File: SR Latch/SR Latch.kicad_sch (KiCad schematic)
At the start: 15 parts, among them J1 Conn_01x02, Q1 BC547, Q2 BC547, Q3 BC547, Q4 BC547, SW1 RESET, SW2 SET

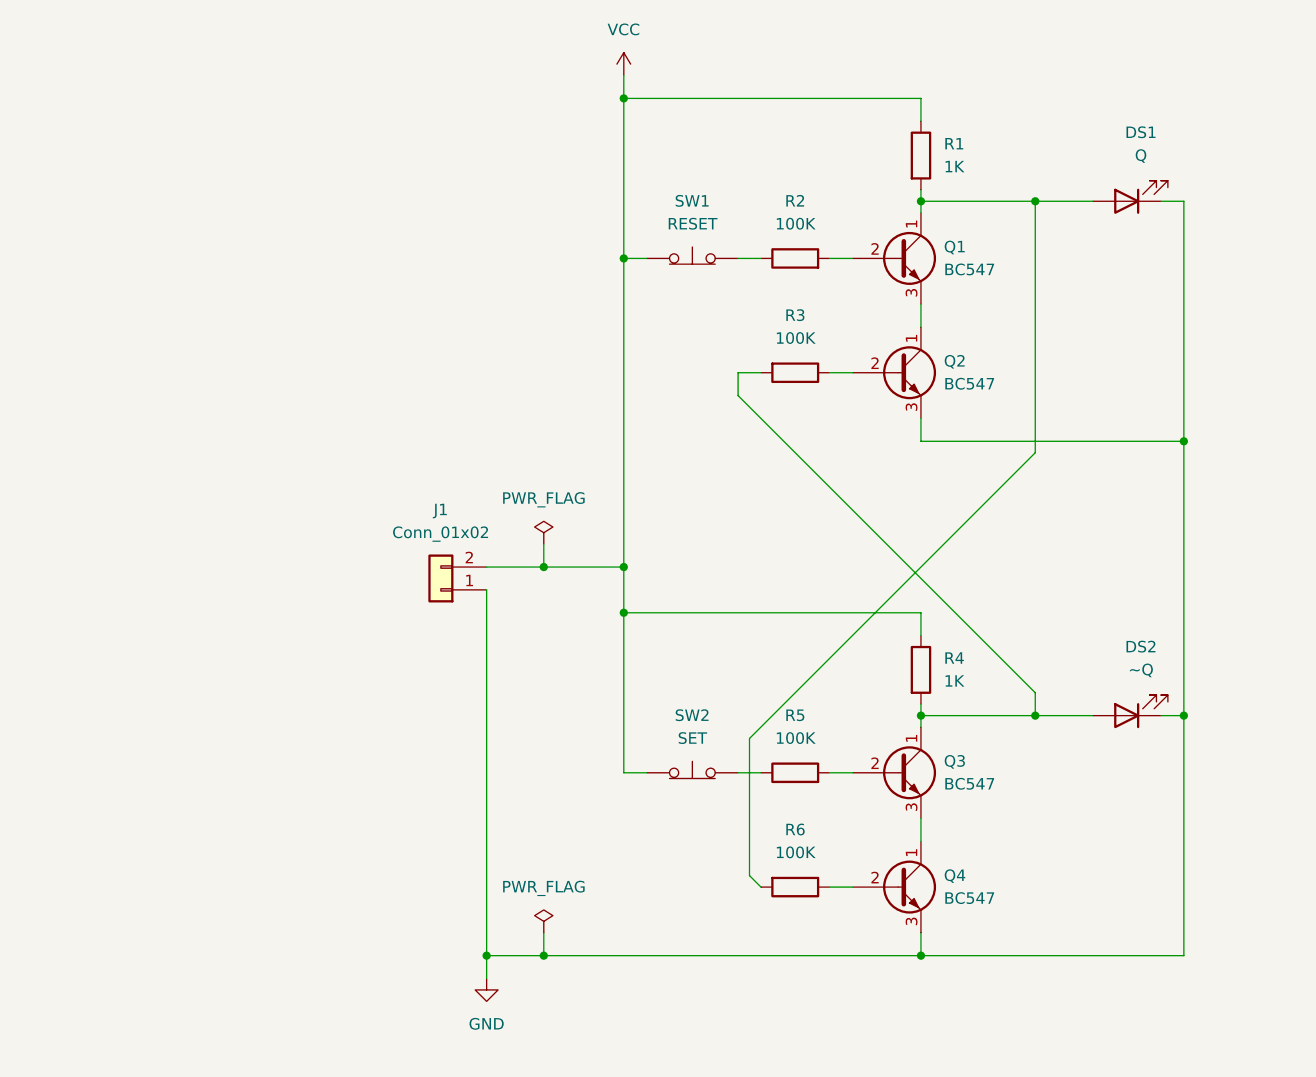
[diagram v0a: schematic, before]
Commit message: fix(SR Latch): Updated resistor values
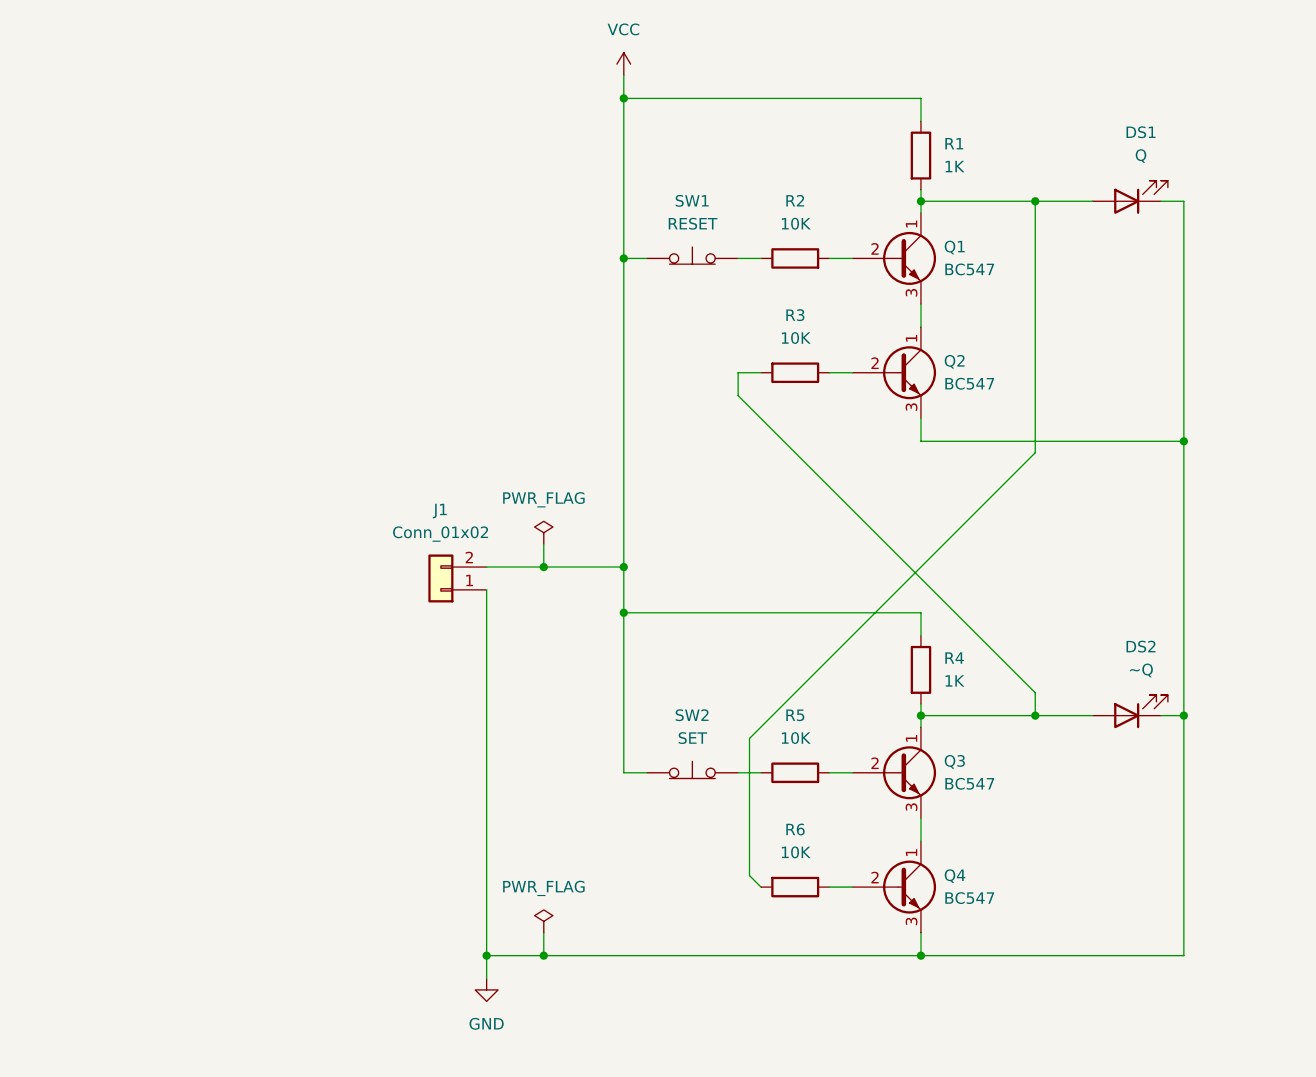
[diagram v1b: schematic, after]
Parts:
- R2, R3, R5, R6: value 100K -> 10K
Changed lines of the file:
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@@
       (effects (font (size 1.27 1.27)))
     )
-    (property "Value" "100K" (at 148.59 127 90)
+    (property "Value" "10K" (at 148.59 127 90)
       (effects (font (size 1.27 1.27)))
     )
@@
       (effects (font (size 1.27 1.27)))
     )
-    (property "Value" "100K" (at 148.59 114.3 90)
+    (property "Value" "10K" (at 148.59 114.3 90)
       (effects (font (size 1.27 1.27)))
     )
@@
       (effects (font (size 1.27 1.27)))
     )
-    (property "Value" "100K" (at 148.59 57.15 90)
+    (property "Value" "10K" (at 148.59 57.15 90)
       (effects (font (size 1.27 1.27)))
     )
@@
       (effects (font (size 1.27 1.27)))
     )
-    (property "Value" "100K" (at 148.59 69.85 90)
-      (effects (font (size 1.27 1.27)))
-    )
+    (property "Value" "10K" (at 148.59 69.85 90)
+      (effects (font (size 1.27 1.27)))
+    )

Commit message: fix: Fixed the SR Latch project (Omron tactile switches)
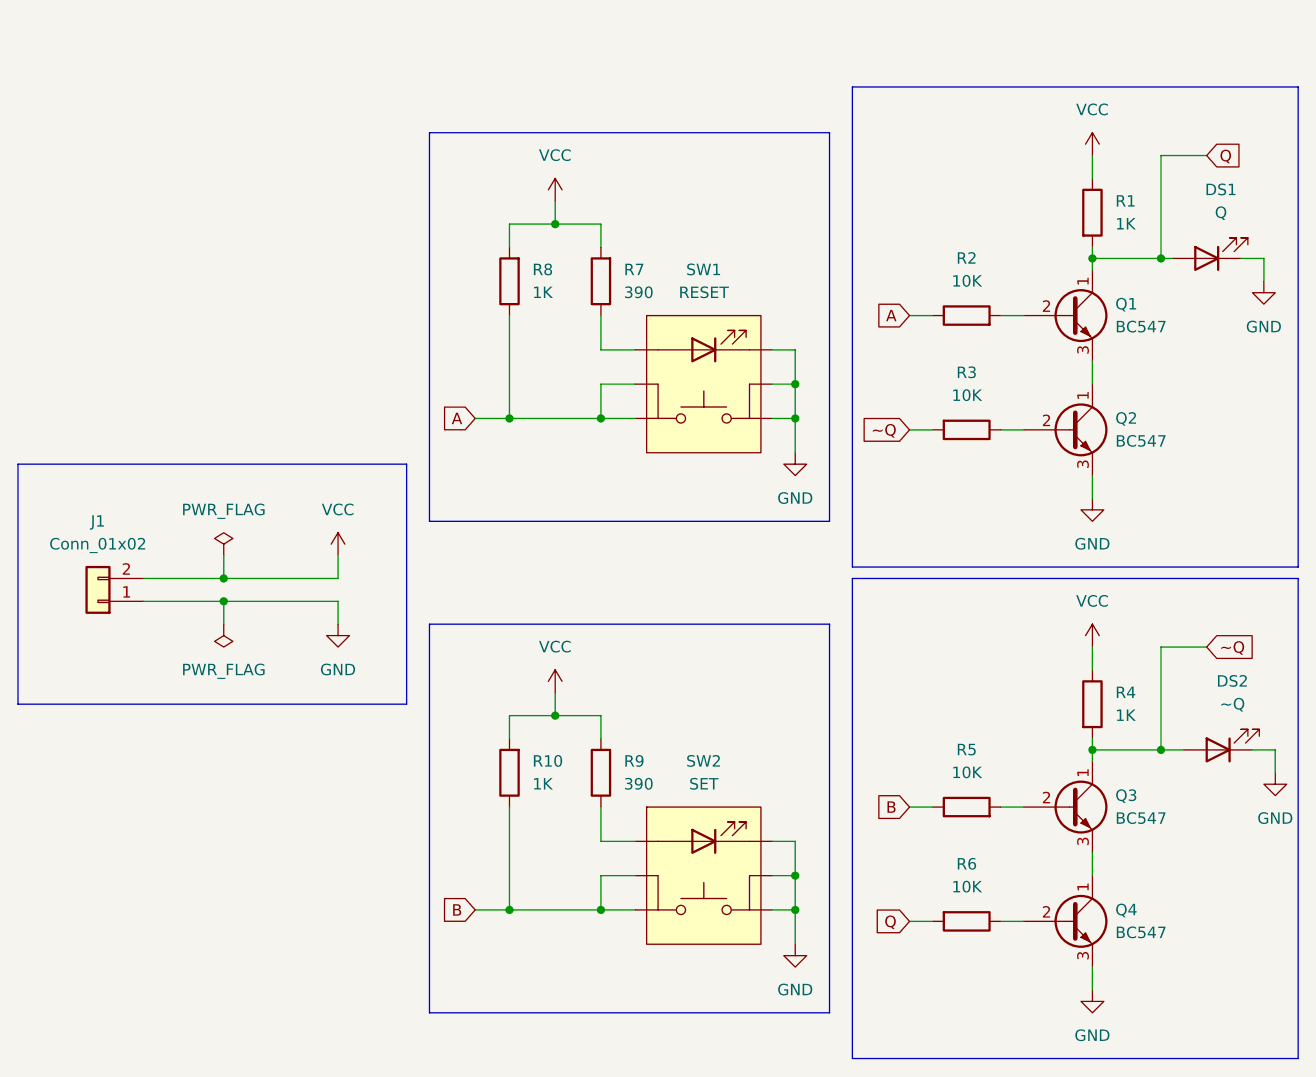
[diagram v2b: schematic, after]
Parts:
- removed SW1: RESET, XS:Tactile-Omrom-B3W-900X-X1X, symbol Switch:SW_Push_Open
- removed SW2: SET, XS:Tactile-Omrom-B3W-900X-X1X, symbol Switch:SW_Push_Open
- added R10, R8: 1K, XS:Resistor-Vishay-CCF07, symbol Device:R
- added R7, R9: 390, XS:Resistor-Vishay-CCF07, symbol Device:R
- added SW1: RESET, XS:Tactile-Omron-B3W-900X-X1X, symbol XS:Tactile-Omron-B3W-900X-X1X
- added SW2: SET, XS:Tactile-Omron-B3W-900X-X1X, symbol XS:Tactile-Omron-B3W-900X-X1X
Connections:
- net GND: now also SW1.1, SW1.2, SW1.5 (K), SW2.1, SW2.2, SW2.5 (K)
- net VCC: now also R10.2, R7.2, R8.2, R9.2
- net Q: now reaches DS1.2 (A), Q1.1 (C), R1.2, R6.2
- net B: now reaches R5.1
- net B: now also R10.1, SW2.3, SW2.4
- net A: now reaches R2.1
- net A: now also R8.1, SW1.3, SW1.4
- net ~Q: now reaches DS2.2 (A), Q3.1 (C), R3.2, R4.2
- new net: R7.1, SW1.6 (A)
- new net: R9.1, SW2.6 (A)
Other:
- moved on the sheet: DS1, DS2, J1, Q1, Q2, Q3, Q4, R1, R2, R3, R4, R5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

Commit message: chore: Using D for LEDs instead of DS
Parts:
- renumbered DS1 to D1, DS2 to D2
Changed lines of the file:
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@@
   (symbol (lib_id "Device:LED") (at 195.58 115.57 180) (unit 1)
     (in_bom yes) (on_board yes) (dnp no) (fields_autoplaced)
-    (property "Reference" "DS2" (at 197.1675 107.95 0)
+    (property "Reference" "D2" (at 197.1675 107.95 0)
       (effects (font (size 1.27 1.27)))
     )
@@
       (project "SR Latch"
         (path "/216a0792-1cac-4e9e-9a5e-17e3ce501423"
-          (reference "DS2") (unit 1)
+          (reference "D2") (unit 1)
         )
       )
@@
   (symbol (lib_id "Device:LED") (at 194.31 60.96 180) (unit 1)
     (in_bom yes) (on_board yes) (dnp no) (fields_autoplaced)
-    (property "Reference" "DS1" (at 195.8975 53.34 0)
+    (property "Reference" "D1" (at 195.8975 53.34 0)
       (effects (font (size 1.27 1.27)))
     )
@@
       (project "SR Latch"
         (path "/216a0792-1cac-4e9e-9a5e-17e3ce501423"
-          (reference "DS1") (unit 1)
+          (reference "D1") (unit 1)
         )
       )

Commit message: fix: SR Latch - Fixed the SET/RESET labels
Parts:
- SW1: value RESET -> SET
- SW2: value SET -> RESET
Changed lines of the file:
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@@
       (effects (font (size 1.27 1.27)))
     )
-    (property "Value" "RESET" (at 138.43 64.77 0)
+    (property "Value" "SET" (at 138.43 64.77 0)
       (effects (font (size 1.27 1.27)))
     )
@@
       (effects (font (size 1.27 1.27)))
     )
-    (property "Value" "SET" (at 138.43 119.38 0)
-      (effects (font (size 1.27 1.27)))
-    )
+    (property "Value" "RESET" (at 138.43 119.38 0)
+      (effects (font (size 1.27 1.27)))
+    )
